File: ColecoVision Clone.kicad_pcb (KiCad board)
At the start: 2 copper layers, 149.4 x 99.1 mm, 141 parts, among them J1 Cartridge Slot, J2 Composite video, J3 PJ-102A, J4 RCJ-017, J5 Controller Port 1, J6 Controller Port 2, Q1 2n4401, Q2 Q_NJFET_GSD, Q3 2N3906, Q4 2N3904, Q5 2N3904, SW1 Power Toggle, SW2 Reset, U1 PLCCZ80, U10 SN76489AN, U11 74LS04, U12 74LS138 (Mem. Mapped), U13 74LS138 (I/O), U14 74LS02, U15 Controller 1, U16 Controller 2, U17 74LS05, U18 74LS05, U2 Work RAM, U20 74LS74, U22 74LS74, U23 74HCT00, U24 TPS60403DBVR, U3 BIOS ROM 27C256, U4 74HCT04, U5 TMS9918A, U6 74LS574, U7 74LS574, U8 74LS574, U9 VRAM, X1 14.31818MHz, Y1 10.738635MHZ

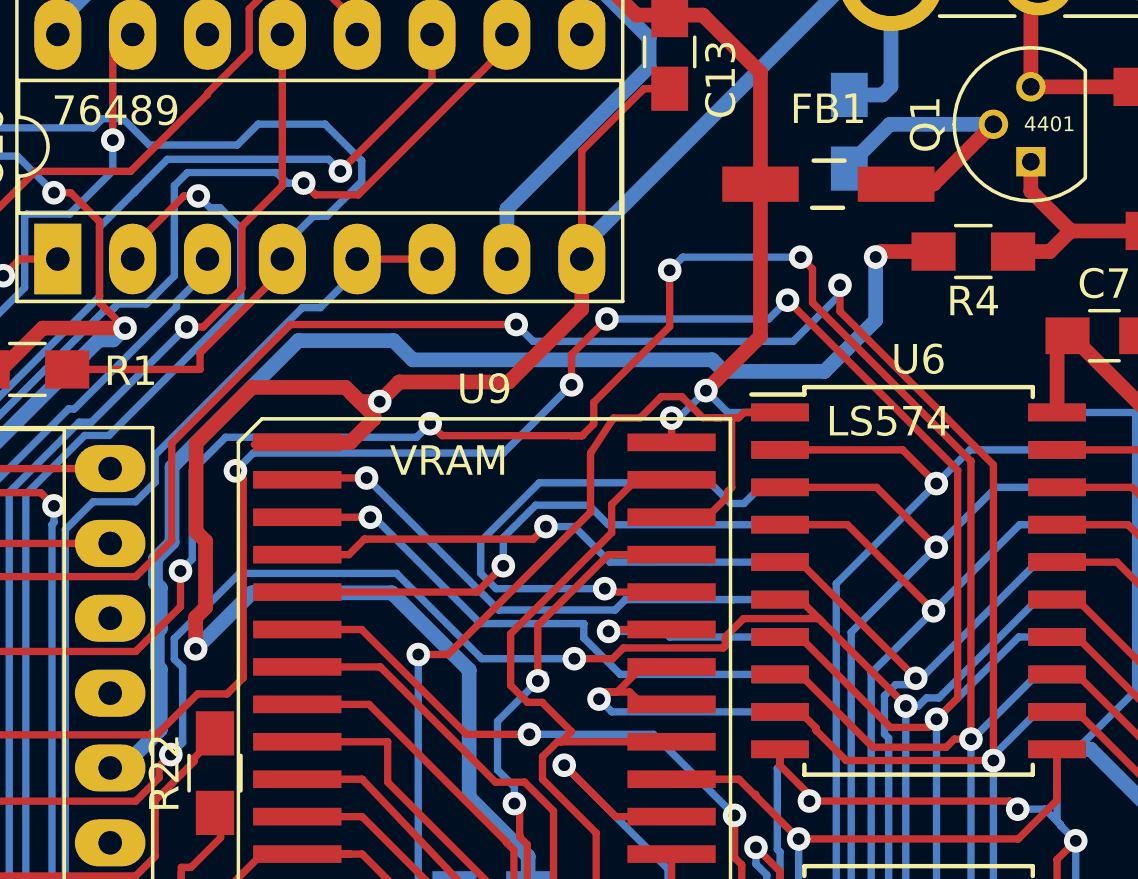
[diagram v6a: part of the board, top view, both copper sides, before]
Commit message: A tough-won via removal
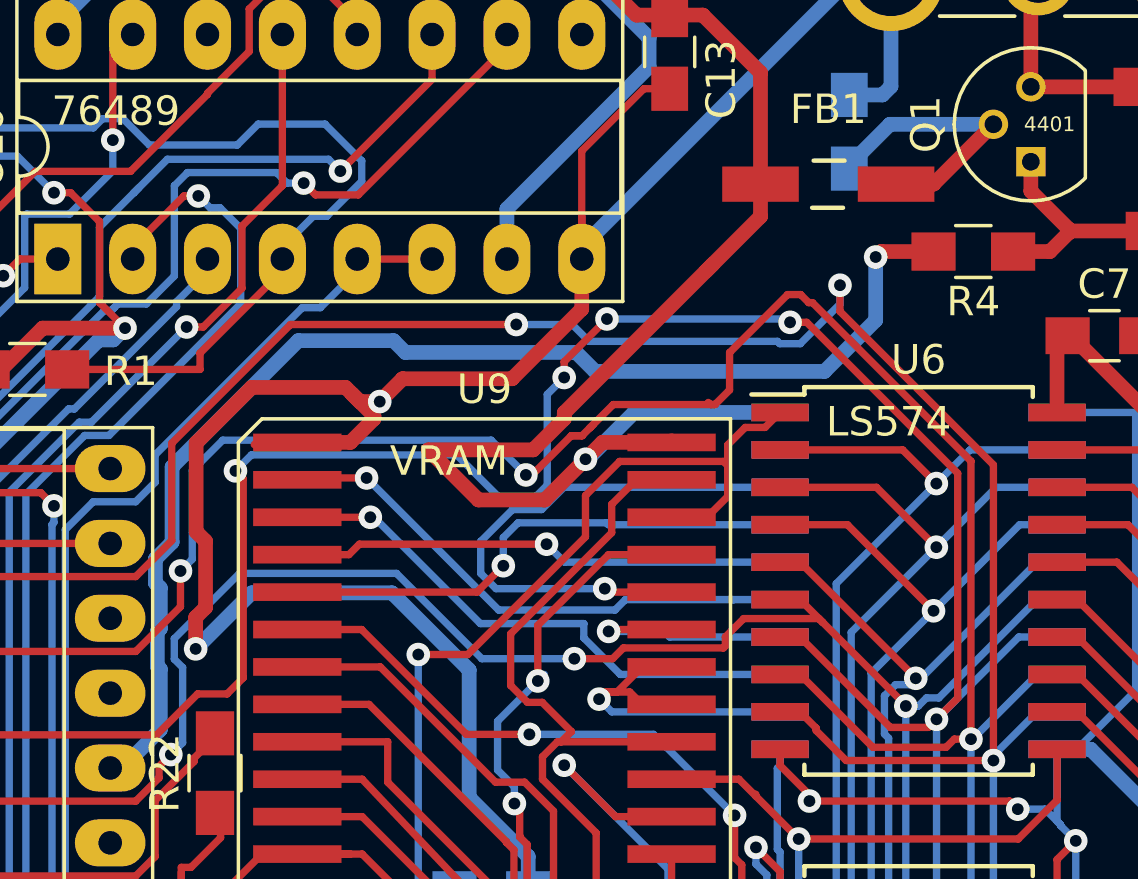
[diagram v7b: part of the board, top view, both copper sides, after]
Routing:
- net VCC: track 871.7 -> 892.1 mm, vias 49 -> 48
- net RW: track 84.3 -> 82.1 mm
- net AD5: track 91.6 -> 93.7 mm
- net AD6: track 90.0 -> 88.5 mm, vias 6 -> 4
- net RAM_A7: track 19.4 -> 18.8 mm

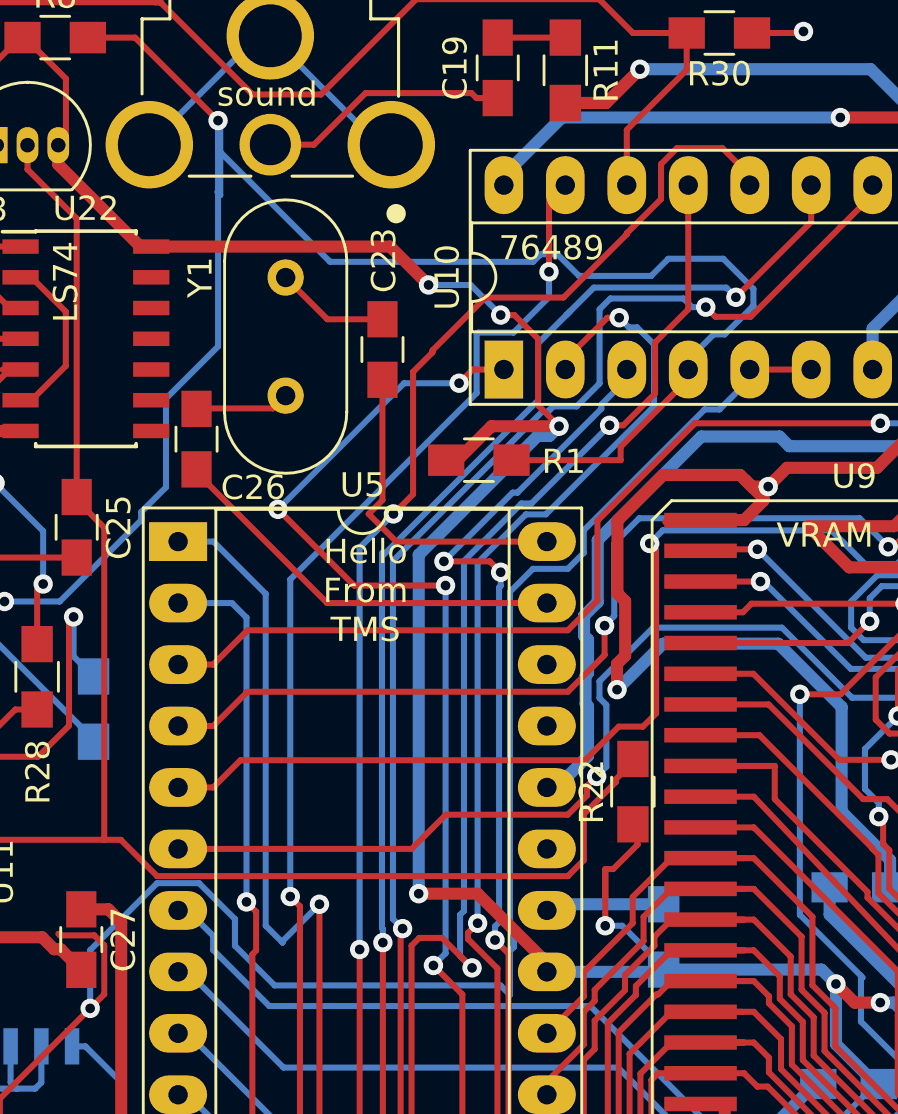
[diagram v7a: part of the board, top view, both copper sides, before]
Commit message: Cleaning up power via
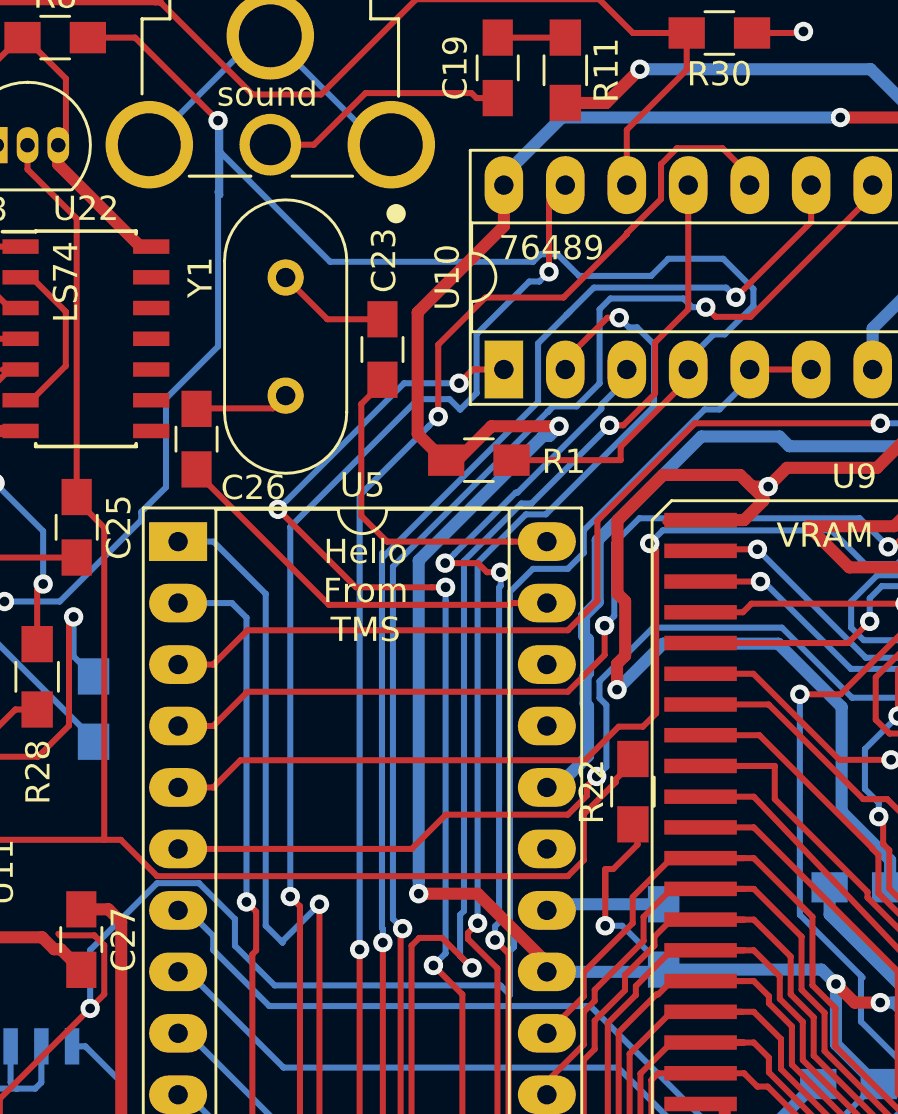
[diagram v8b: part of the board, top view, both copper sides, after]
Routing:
- net VCC: track 892.1 -> 883.8 mm, vias 48 -> 46
- net D4: track 294.9 -> 295.9 mm
